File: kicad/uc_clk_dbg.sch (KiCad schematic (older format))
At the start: 18 parts, among them U1_? TMS320F28388DZWTS

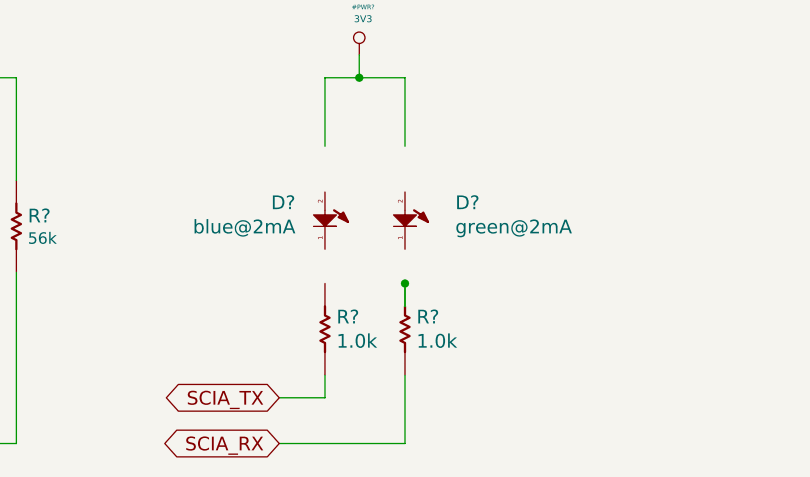
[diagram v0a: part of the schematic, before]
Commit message: added isolated gpi, change digital iso gpo from 2 to 8
I've found some Silabs IC's that match better than texas, are cheaper
and on stock. For digital isolation the GPIO to IGBT and data input from
QRP  and GPI from external switches.
I'm adding these IC's and clean the schematics a lots.
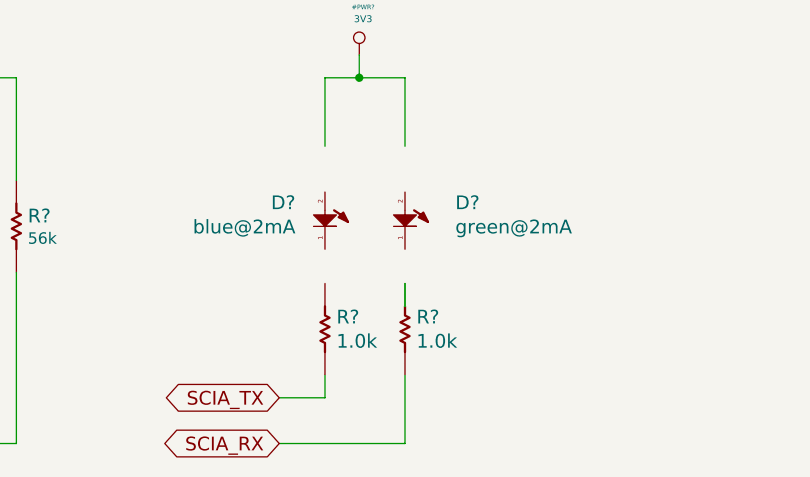
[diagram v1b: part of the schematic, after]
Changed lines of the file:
@@
 $Descr A4 11693 8268
 encoding utf-8
-Sheet 6 17
+Sheet 6 18
 Title "clk"
 Date "25 10 2019"
@@
 	1    0    0    -1
 $EndComp
-Connection ~ 6050 5000
 $Comp
 L Connector_Generic:Conn_02x05_Counter_Clockwise J?

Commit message: added buffers and leds 2 igbt. added xtal for PHY's
I've added one xtal for each PYH instead/appart of the uC pin to drive
the clk for thouse IC's. If the uC could manage to clk them, just
depoppulate the xtal, if not, 3 xtal will be needed. But I guess is
better than distribuiton of 25Mhz between IC's, even they were
buffered...
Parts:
- removed TP?: ~, symbol servo:CMP-0078143-2
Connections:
- wire segments 66 -> 64
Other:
- moved on the sheet: D?, R?

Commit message: improve ethercat, embedded rj45 to spare, remove some unnecesary r's
I've worked on ethetcat/net to improve visibility on A3 page and also
remove some R's related to leds and change the embedded Rj45 for the
spare transformer and connector 'cause half the price and more options
to choose the connector shape and position
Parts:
- removed J?: Conn_02x05_Counter_Clockwise, symbol Connector_Generic:Conn_02x05_Counter_Clockwise
- added C?: 0.1uF, symbol servo:Capacitor
- added J?: Conn_02x05_Counter_Clockwise, symbol Connector_Generic:Conn_02x05_Counter_Clockwise
- added U: M25PX32-VMW, Package_SO:SOIJ-8_5.3x5.3mm_P1.27mm, symbol servo:M25PX32-VMW
- added U?: SN74ALVC244PW, symbol servo:SN74ALVC244PW
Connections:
- net labels added: FLASH_SPI_CLK, FLASH_SPI_CS, FLASH_SPI_MISO, FLASH_SPI_MOSI
- wire segments 64 -> 124
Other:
- note added: "SPI FLASH"
- note added: "To store some firmware features, \nand maybe UI images or screens"
- moved on the sheet: C?, D?, R?, S?, U1_?C, Y?

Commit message: remove isolation GPIO's and replace it by free pins at IGBT
I remove completely the isolated inputs pins cause I've 8 pins free at
IGBT isolated interfase, so I leave 4 for outpus and 4 for inputs with
one isolated stage, the same as the previous isolated GPIO sheet..
I've improved the DBG sheet and some other details,. I'm ready to make
some electrical checks and fchoose the parts codes and footprints.. go
for it!
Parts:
- added C?: 1nF, symbol servo:Capacitor
- added J?: Screw_Terminal_01x02, symbol Connector:Screw_Terminal_01x02
- added R? (x2): 680, symbol servo:Resistor
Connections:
- net labels added: DACB_DBG_OUT, PRG_SCI_RX, PRG_SCI_TX, PRG_TCK, PRG_TDI, PRG_TDO, PRG_TMS, PRG_TRSTn
- wire segments 124 -> 106
- no-connect marks 2 -> 3
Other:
- note added: "BOOTSRAP R's"
- note added: "CLK + JTAG + SCI\n"
- note added: "DAC DBG OUT"
- note added: "I left fixed in flash mode\nif you need to change it you'll get dirty\n\n"
- note added: "MULTI PORPOUSE \nLEDS"
- note added: "Programmer connector plus SCI for debug porpouses.. take in account\n that it's not isolated, only buffered to minimize risk. It's supoussed that\n th 3v3 cold side never touch 220v\n"
- note added: "it's just optional for debug porpouses to monitor\n some analog signal out from the board, it could \nbe very handy"
- note removed: "Boot Mode to\n Flash/USB\n"
- note removed: "IDC connector to plug \nan external isolated jtag interface"
- note removed: "Multipropouse\nLEDs"
- note removed: "SCI leds\n"
- moved on the sheet: C?, D?, J?, R?, S?, U, U1_?C, U?, Y?

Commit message: added 4 push buttons and more gpios on LCD connector
just to have more UI options. With those I'd manage graphics LCD plus 4
buttons, and charaveter LCD. or the embedded EVE graphic LCD
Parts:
- removed D? (x2): red@2mA, symbol servo:LED_A2_K1
- removed R?: 680, symbol servo:Resistor
- added D603, D604: red@2mA, symbol servo:LED_A2_K1
- added R601: 680, symbol servo:Resistor
- gave numbers to parts that had none: 20
- renumbered U to U603
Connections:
- net 3V3: now also U603.3 (W#/VPP), U603.7 (HOLD#), R601.1
- net GND: now also U602.13 (2A2); no longer U602.7 (2Y2)
- net RUN_LED0: now also D603.1 (K)
- net RUN_LED1: now also D604.1 (K)
- net at R602.2: now also D604.2 (A)
- new net: D603.2 (A), R601.2
- no-connect marks 3 -> 8

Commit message: begin PCB!! it's amess but IT IS
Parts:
- C601, C604, C606: footprint (none) -> Capacitor_SMD:C_0603_1608Metric
- R601, R602, R608, R610, R612, R614, R616, R618, R620, R622: footprint (none) -> Resistor_SMD:R_0603_1608Metric
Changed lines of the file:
@@
 F 0 "R622" V 13945 3300 60  0000 R CNN
 F 1 "2.2k" V 13847 3300 50  0000 R CNN
-F 2 "" H 13900 3350 50  0001 C CNN
+F 2 "Resistor_SMD:R_0603_1608Metric" H 13900 3350 50  0001 C CNN
 F 3 "" H 13900 3350 50  0001 C CNN
 F 4 "2.2k" V 11100 1150 60  0001 C CNN "ValueDisplayed"
@@
 F 0 "C604" V 13995 3909 60  0000 L CNN
 F 1 "0.01uF" V 13897 3909 50  0000 L CNN
-F 2 "" H 13900 3800 50  0001 C CNN
+F 2 "Capacitor_SMD:C_0603_1608Metric" H 13900 3800 50  0001 C CNN
 F 3 "" H 13900 3800 50  0001 C CNN
 F 4 "0.01uF" V 11100 900 60  0001 C CNN "ValueDisplayed"
@@
 F 0 "R610" V 6255 7600 60  0000 L CNN
 F 1 "56k" V 6353 7600 50  0000 L CNN
-F 2 "" H 6300 7550 50  0001 C CNN
+F 2 "Resistor_SMD:R_0603_1608Metric" H 6300 7550 50  0001 C CNN
 F 3 "" H 6300 7550 50  0001 C CNN
 F 4 "56k" V -7900 4050 60  0001 C CNN "ValueDisplayed"
@@
 F 0 "R612" V 6645 7500 60  0000 R CNN
 F 1 "56k" V 6547 7500 50  0000 R CNN
-F 2 "" H 6600 7550 50  0001 C CNN
+F 2 "Resistor_SMD:R_0603_1608Metric" H 6600 7550 50  0001 C CNN
 F 3 "" H 6600 7550 50  0001 C CNN
 F 4 "56k" V -7900 4050 60  0001 C CNN "ValueDisplayed"
@@
 F 0 "R601" V 2905 7450 60  0000 L CNN
 F 1 "680" V 3003 7450 50  0000 L CNN
-F 2 "" H 2950 7400 50  0001 C CNN
+F 2 "Resistor_SMD:R_0603_1608Metric" H 2950 7400 50  0001 C CNN
 F 3 "" H 2950 7400 50  0001 C CNN
 F 4 "680" V -5450 8200 60  0001 C CNN "ValueDisplayed"
@@
 F 0 "R616" V 10095 3150 60  0000 R CNN
 F 1 "2.2k" V 9997 3150 50  0000 R CNN
-F 2 "" H 10050 3200 50  0001 C CNN
+F 2 "Resistor_SMD:R_0603_1608Metric" H 10050 3200 50  0001 C CNN
 F 3 "" H 10050 3200 50  0001 C CNN
 F 4 "2.2k" V 9950 2500 60  0001 C CNN "ValueDisplayed"
@@
 F 0 "R602" V 3255 7450 60  0000 L CNN
 F 1 "680" V 3353 7450 50  0000 L CNN
-F 2 "" H 3300 7400 50  0001 C CNN
+F 2 "Resistor_SMD:R_0603_1608Metric" H 3300 7400 50  0001 C CNN
 F 3 "" H 3300 7400 50  0001 C CNN
 F 4 "680" V -5700 8200 60  0001 C CNN "ValueDisplayed"
@@
 F 0 "R614" V 8197 3850 60  0000 L CNN
 F 1 "1.0k" H 8250 3800 50  0001 C CNN
-F 2 "" H 8250 3800 50  0001 C CNN
+F 2 "Resistor_SMD:R_0603_1608Metric" H 8250 3800 50  0001 C CNN
 F 3 "" H 8250 3800 50  0001 C CNN
 F 4 "1.0k" V 8303 3850 60  0000 L CNN "ValueDisplayed"
@@
 F 0 "R608" V 4347 3650 60  0000 L CNN
 F 1 "1.0k" H 4400 3600 50  0001 C CNN
-F 2 "" H 4400 3600 50  0001 C CNN
+F 2 "Resistor_SMD:R_0603_1608Metric" H 4400 3600 50  0001 C CNN
 F 3 "" H 4400 3600 50  0001 C CNN
 F 4 "1.0k" V 4453 3650 60  0000 L CNN "ValueDisplayed"
@@
 F 0 "C606" V 14395 7459 60  0000 L CNN
 F 1 "0.1uF" V 14297 7459 50  0000 L CNN
-F 2 "" H 14300 7350 50  0001 C CNN
+F 2 "Capacitor_SMD:C_0603_1608Metric" H 14300 7350 50  0001 C CNN
 F 3 "" H 14300 7350 50  0001 C CNN
 F 4 "0.1uF" V 11700 7750 60  0001 C CNN "ValueDisplayed"
@@
 F 0 "R618" H 10100 7543 60  0000 C CNN
 F 1 "680" H 10100 7445 50  0000 C CNN
-F 2 "" H 10100 7350 50  0001 C CNN
+F 2 "Resistor_SMD:R_0603_1608Metric" H 10100 7350 50  0001 C CNN
 F 3 "" H 10100 7350 50  0001 C CNN
 F 4 "680" V 1100 8150 60  0001 C CNN "ValueDisplayed"
@@
 F 0 "C601" V 10297 7660 60  0001 L CNN
 F 1 "1nF" V 10403 7660 60  0001 L CNN
-F 2 "" H 10300 7550 60  0000 C CNN
+F 2 "Capacitor_SMD:C_0603_1608Metric" H 10300 7550 60  0000 C CNN
 F 3 "" H 10300 7550 60  0000 C CNN
 	1    10300 7550
@@
 F 0 "R620" H 10500 7543 60  0000 C CNN
 F 1 "680" H 10500 7445 50  0000 C CNN
-F 2 "" H 10500 7350 50  0001 C CNN
+F 2 "Resistor_SMD:R_0603_1608Metric" H 10500 7350 50  0001 C CNN
 F 3 "" H 10500 7350 50  0001 C CNN
 F 4 "680" V 1500 8150 60  0001 C CNN "ValueDisplayed"

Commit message: I've passed all footprin to layout BUT...
I've passed all, first glance... I need to confirm in details a lot of
things. The objetive for these is to have an aproximation of the size
I'll need to make the board.. then I choose the final detailed footprint
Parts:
- removed J602: Screw_Terminal_01x02, symbol Connector:Screw_Terminal_01x02
- removed S601: ~, symbol servo:Switch_PushButton_GND3
- added J602: Conn_01x02, Connector_PinHeader_2.54mm:PinHeader_1x02_P2.54mm_Vertical_SMD_Pin1Left, symbol servo:Conn_01x02
- added TP601: TestPoint, TestPoint:TestPoint_Loop_D2.50mm_Drill1.0mm, symbol servo:TestPoint
- C601: footprint Capacitor_SMD:C_0603_1608Metric -> servo:C_0603_1608Metric
- C602: renamed from C604; footprint Capacitor_SMD:C_0603_1608Metric -> servo:C_0603_1608Metric
- C603: renamed from C606; footprint Capacitor_SMD:C_0603_1608Metric -> servo:C_0603_1608Metric
- D601: renamed from D603; value red@2mA -> blue@2mA; footprint (none) -> servo:LED_0603_1608Metric
- D602: renamed from D604; value red@2mA -> blue@2mA; footprint (none) -> servo:LED_0603_1608Metric
- D603: renamed from D605; footprint (none) -> servo:LED_0603_1608Metric
- D604: renamed from D606; footprint (none) -> servo:LED_0603_1608Metric
- J601: footprint (none) -> Connector_IDC:IDC-Header_2x05_P2.54mm_Vertical
- U1_501: footprint (none) -> servo:BGA337CP80_19X19_1600X1600X140B50N
- U601: renamed from U602; footprint (none) -> Package_SO:TSSOP-20_4.4x6.5mm_P0.65mm
- Y601: footprint (none) -> Oscillator:Oscillator_SMD_SeikoEpson_SG210-4Pin_2.5x2.0mm
- renumbered R608 to R603, R610 to R604, R612 to R605, R614 to R606, R616 to R607, R618 to R608, R620 to R609, R622 to R610, U603 to U602
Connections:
- net 3V3: now also C603.2 (Capacitor), R605.1; no longer C603.1, R605.2
- net BOOT2: now also R605.2; no longer R605.1
- net GND: now also C603.1, J602.2 (Pin_2); no longer C603.2 (Capacitor)
- net MCU_XRSn: now also TP601.1
- net at R609.2: now also J602.1 (Pin_1)
